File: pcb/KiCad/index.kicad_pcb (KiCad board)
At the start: 2 copper layers, 64 x 80 mm, 22 parts

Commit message: small update to PCB and add TODO.md
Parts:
- removed the CBYPASS at (85.0, 66.0)
- added CBYPASS: 0.1uF, tscircuit:capacitor_C_Disc_D5.0mm_W2.5mm_P5.00mm, F.Cu at (93.0, 66.0)
- C1, C2, C3, C4: footprint tscircuit:capacitor_axial -> tscircuit:capacitor_C_Disc_D5.0mm_W2.5mm_P5.00mm
- RRESET1: value 4.7kΩ -> 10kΩ
- moved C5 8.00 mm to (123.0, 66.0)
- moved RFB 8.00 mm to (98.0, 66.0)
- moved RPULL 8.00 mm to (128.0, 66.0)
- moved RSERIES 8.00 mm to (118.0, 66.0)
- moved U5 8.00 mm to (108.0, 66.0)
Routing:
- net D6: track 47.0 -> 80.7 mm, vias 0 -> 1
- net VCC: track 177.5 -> 146.6 mm
- net D2: track 58.4 -> 75.7 mm
- net A14: track 61.0 -> 74.9 mm
- net A2: track 27.1 -> 37.0 mm, vias 1 -> 0
- net A3: track 27.3 -> 37.0 mm, vias 1 -> 0
- net D1: track 67.1 -> 61.7 mm, vias 2 -> 1
- net D5: track 41.9 -> 45.4 mm
- net D4: track 41.9 -> 45.4 mm
- net D7: track 47.2 -> 50.5 mm
- net A7: track 30.1 -> 26.9 mm, vias 1 -> 0
- net A12: track 41.4 -> 38.4 mm, vias 1 -> 0
- net D3: track 63.1 -> 65.3 mm, vias 1 -> 0
- net A10: track 11.7 -> 13.4 mm, vias 0 -> 1
- net PHI2: track 38.8 -> 40.3 mm
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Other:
- board text added: "github.com/jbsohn/lokey-7800-ym"

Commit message: cleanup pcb build
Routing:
- net A14: track 74.9 -> 109.4 mm
- net D6: track 80.7 -> 47.0 mm, vias 1 -> 0
- net D3: track 65.3 -> 50.0 mm
- net A2: track 37.0 -> 26.9 mm, vias 0 -> 1
- net A15: track 56.0 -> 65.8 mm, vias 2 -> 0
- net A3: track 37.0 -> 27.8 mm, vias 0 -> 1
- net DA7: track 38.2 -> 31.7 mm
- net VCC: track 146.6 -> 140.3 mm
- net A12: track 38.4 -> 44.3 mm
- net D2: track 75.7 -> 70.5 mm
- net D5: track 45.4 -> 41.9 mm
- net D4: track 45.4 -> 41.9 mm
- net A5: track 26.9 -> 28.9 mm, vias 0 -> 1
- net A13: track 15.1 -> 17.1 mm, vias 0 -> 1
- net A10: track 13.4 -> 11.7 mm, vias 1 -> 0
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
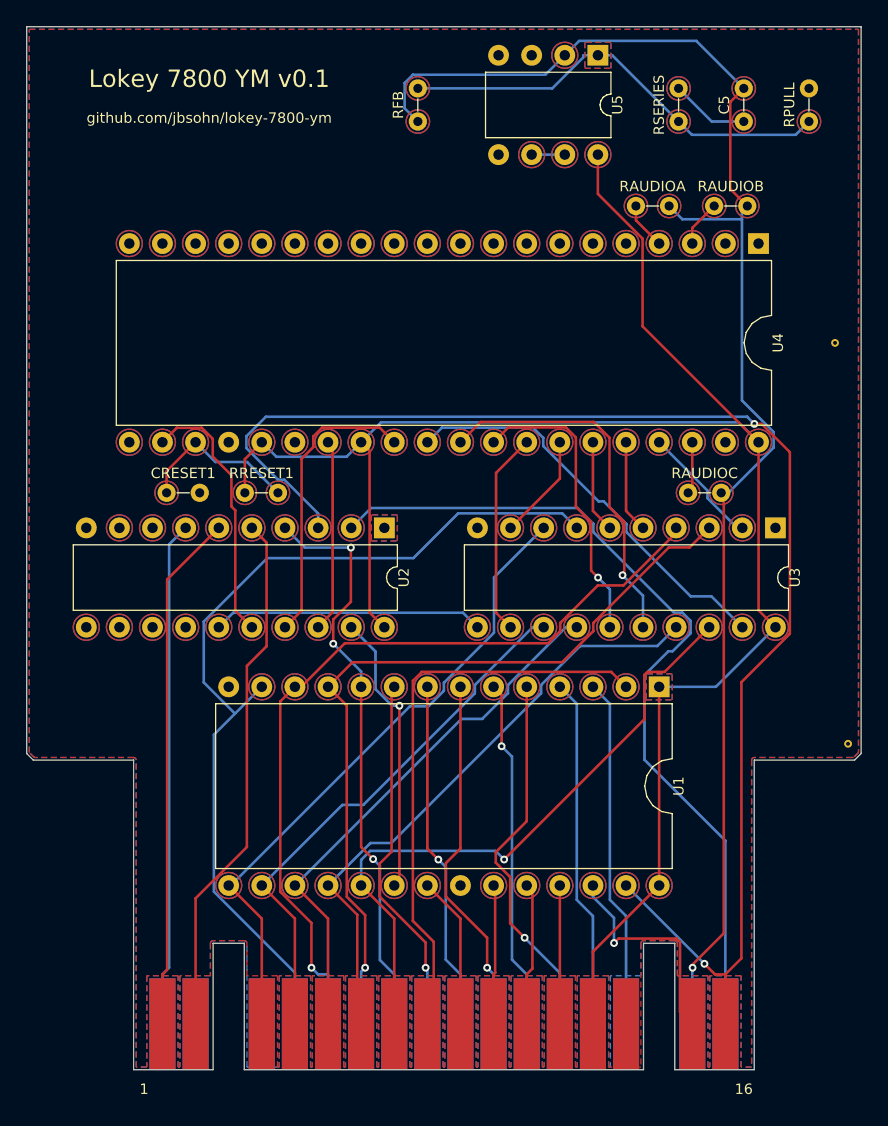
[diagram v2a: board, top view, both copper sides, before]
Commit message: fix opamp setting to match prototype
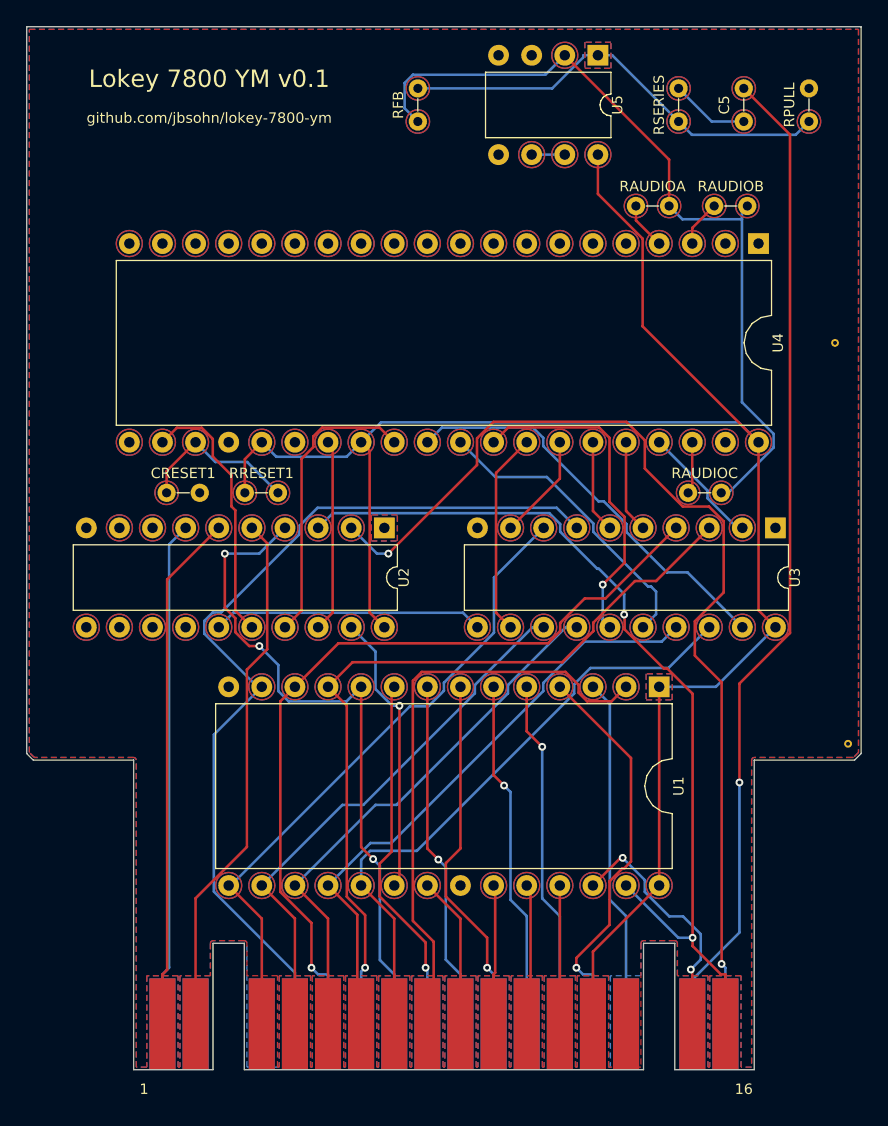
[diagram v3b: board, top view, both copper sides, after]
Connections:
- C5 pad 2: SUM_NODE -> OPAMP_OUT_AC
- J1 pad 18: SUM_NODE -> OPAMP_OUT_AC
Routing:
- net OPAMP_OUT_AC: track 0.00 -> 76.3 mm, vias 0 -> 1
- net SUM_NODE: track 115.2 -> 62.6 mm, vias 1 -> 0
- net A14: track 109.4 -> 70.2 mm
- net A15: track 65.8 -> 79.6 mm, vias 0 -> 2
- net A0: track 44.7 -> 52.2 mm
- net DA6: track 28.3 -> 23.3 mm, vias 1 -> 0
- net A6: track 26.9 -> 30.9 mm, vias 0 -> 1
- net DA5: track 22.7 -> 25.6 mm
- net A13: track 17.1 -> 19.4 mm, vias 1 -> 2
- net D7: track 50.3 -> 48.1 mm, vias 1 -> 0
- net A5: track 28.9 -> 26.9 mm
- net A12: track 44.3 -> 45.6 mm

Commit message: cleanup and optimize pcb build, setup for macOS
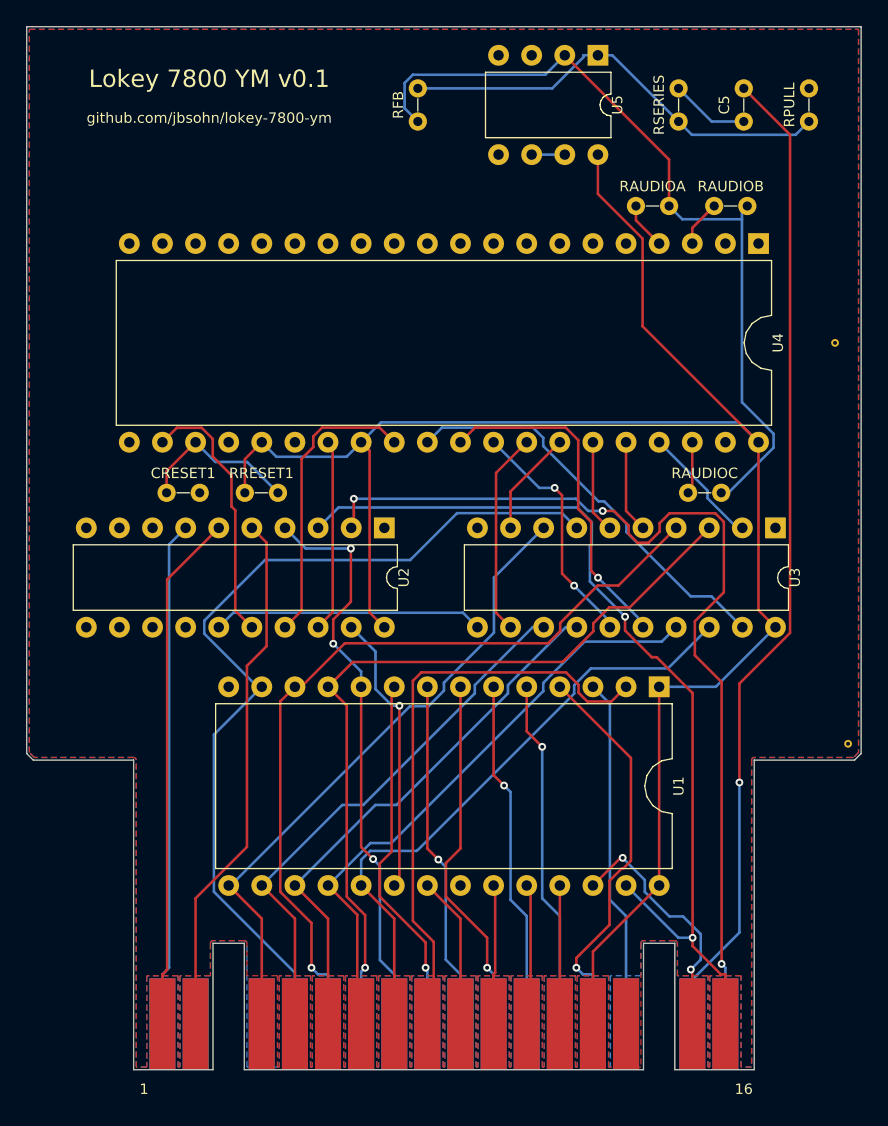
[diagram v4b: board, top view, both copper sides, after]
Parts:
- renumbered CBYPASS to C6, gnd_via to U6, gnd_via2 to U7
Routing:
- net A0: track 52.2 -> 44.7 mm
- net DA5: track 25.6 -> 18.6 mm, vias 1 -> 2
- net A15: track 79.6 -> 74.5 mm, vias 2 -> 3
- net DA6: track 23.3 -> 26.3 mm, vias 0 -> 1
- net A14: track 70.2 -> 72.2 mm
- net D2: track 70.2 -> 69.5 mm
